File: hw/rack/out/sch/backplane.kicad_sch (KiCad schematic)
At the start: 0 parts

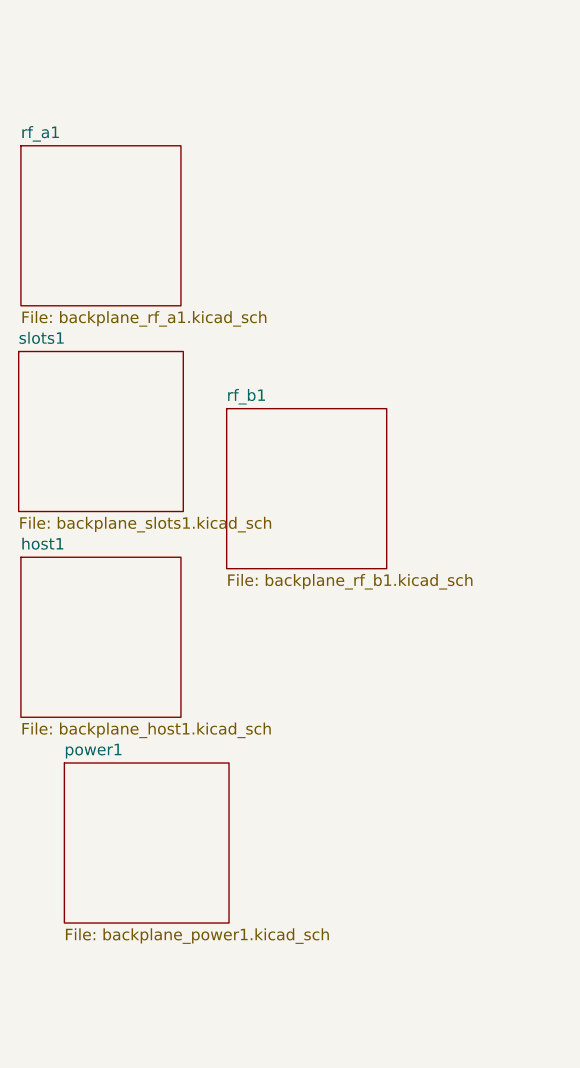
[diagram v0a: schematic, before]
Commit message: hw/rack: #95 review fixes: QPQ1907 pinout + RF continuity test, 1 ohm 2512 bias-T, input fuse, keyed slots, CM4 source, CI scikit-rf + stale check, ADR-0018 gain-plan stop-and-ask (#33)
- QPQ1907 pins per datasheet 040820 (1 in, 4 out, 2/3/5 GND); test walks BNC to every slot port
- bias-T 1 ohm 2512 (0.27 W at 0.52 A), resistor power ratings asserted
- 4 A fuse ahead of the TVS; Harwin M20-7831346 + M20-003 key at position 14
- CM4002008 from The Pi Hut (GBP 79.20); Lite-On LEDs
- Wilkinson +-10 % width sweep; netlist timestamp stripped
- CI: scikit-rf installed, cross-check required under CI, hw/rack stale-output diff
- Audit 6: per-carrier NF, stage headroom at 0.5/1/1.5 m (wings), phones, nRF5340 PS v1.1
  C/I + PIMD, nRF21540 P1dB; no fixed gain plan meets both: stop-and-ask

Co-Authored-By: Claude Opus 5.5 <noreply@anthropic.com>
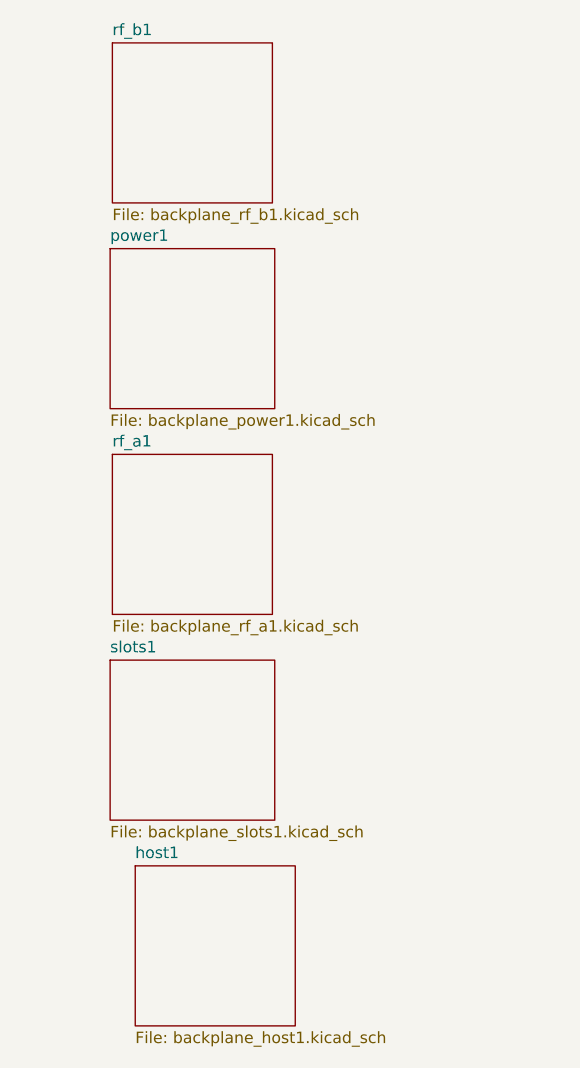
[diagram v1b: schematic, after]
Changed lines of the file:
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@@
     (comment 4 ""))
   (sheet
-    (at 133.1 130.81)
+    (at 138.18 73.66)
     (size 18.29 17.78)
     (exclude_from_sim no)
@@
       (color 0 0 0 0.0))
     (property "Sheetname" "power1"
-      (at 133.1 130.1 0)
+      (at 138.18 72.95 0)
       (effects
         (font
@@
         (justify left bottom)))
     (property "Sheetfile" "backplane_power1.kicad_sch"
-      (at 133.1 149.17 0)
+      (at 138.18 92.02 0)
       (effects
         (font
@@
         (justify left top))))
   (sheet
-    (at 128.27 107.95)
+    (at 140.97 142.24)
     (size 17.78 17.78)
     (exclude_from_sim no)
@@
       (color 0 0 0 0.0))
     (property "Sheetname" "host1"
-      (at 128.27 107.24 0)
+      (at 140.97 141.53 0)
       (effects
         (font
@@
         (justify left bottom)))
     (property "Sheetfile" "backplane_host1.kicad_sch"
-      (at 128.27 126.31 0)
+      (at 140.97 160.6 0)
       (effects
         (font
@@
         (justify left top))))
   (sheet
-    (at 128.27 62.23)
+    (at 138.43 96.52)
     (size 17.78 17.78)
     (exclude_from_sim no)
@@
       (color 0 0 0 0.0))
     (property "Sheetname" "rf_a1"
-      (at 128.27 61.52 0)
+      (at 138.43 95.81 0)
       (effects
         (font
@@
         (justify left bottom)))
     (property "Sheetfile" "backplane_rf_a1.kicad_sch"
-      (at 128.27 80.59 0)
+      (at 138.43 114.88 0)
       (effects
         (font
@@
         (justify left top))))
   (sheet
-    (at 151.13 91.44)
+    (at 138.43 50.8)
     (size 17.78 17.78)
     (exclude_from_sim no)
@@
       (color 0 0 0 0.0))
     (property "Sheetname" "rf_b1"
-      (at 151.13 90.73 0)
+      (at 138.43 50.09 0)
       (effects
         (font
@@
         (justify left bottom)))
     (property "Sheetfile" "backplane_rf_b1.kicad_sch"
-      (at 151.13 109.8 0)
+      (at 138.43 69.16 0)
       (effects
         (font
@@
         (justify left top))))
   (sheet
-    (at 128.02 85.09)
+    (at 138.18 119.38)
     (size 18.29 17.78)
     (exclude_from_sim no)
@@
       (color 0 0 0 0.0))
     (property "Sheetname" "slots1"
-      (at 128.02 84.38 0)
+      (at 138.18 118.67 0)
       (effects
         (font
@@
         (justify left bottom)))
     (property "Sheetfile" "backplane_slots1.kicad_sch"
-      (at 128.02 103.45 0)
+      (at 138.18 137.74 0)
       (effects
         (font
